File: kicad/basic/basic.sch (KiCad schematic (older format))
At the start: 20 parts, among them P2 CONN_01X15, P3 CONN_01X15, P4 CONN_01X06, P5 CONN_01X01, P6 CONN_01X01, P7 CONN_01X01, P8 CONN_01X01, P9 CONN_01X06, SW1 SW_PUSH, SW2 SW_PUSH

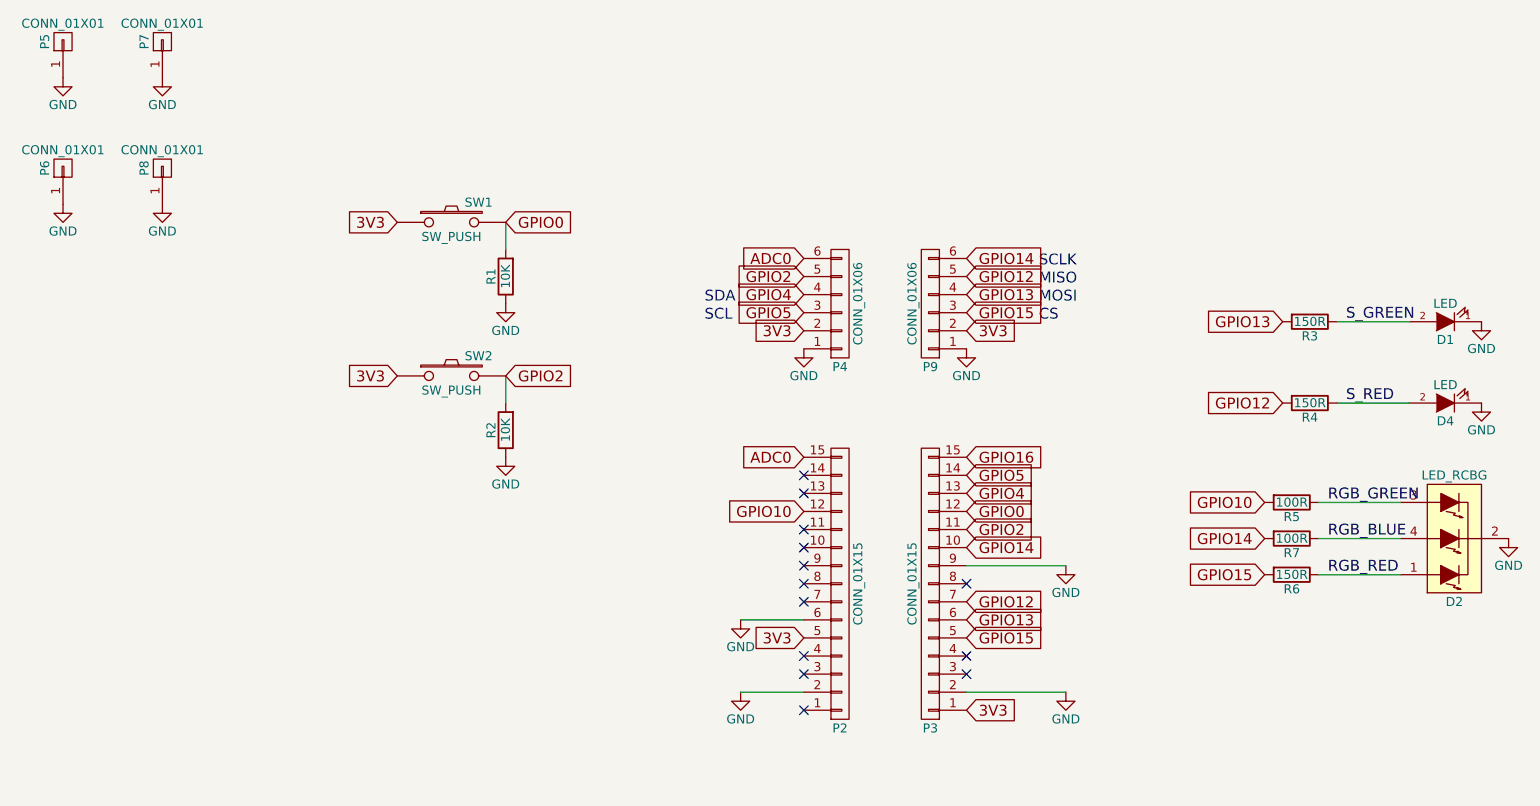
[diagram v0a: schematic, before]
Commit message: I2C & SPI on the headers
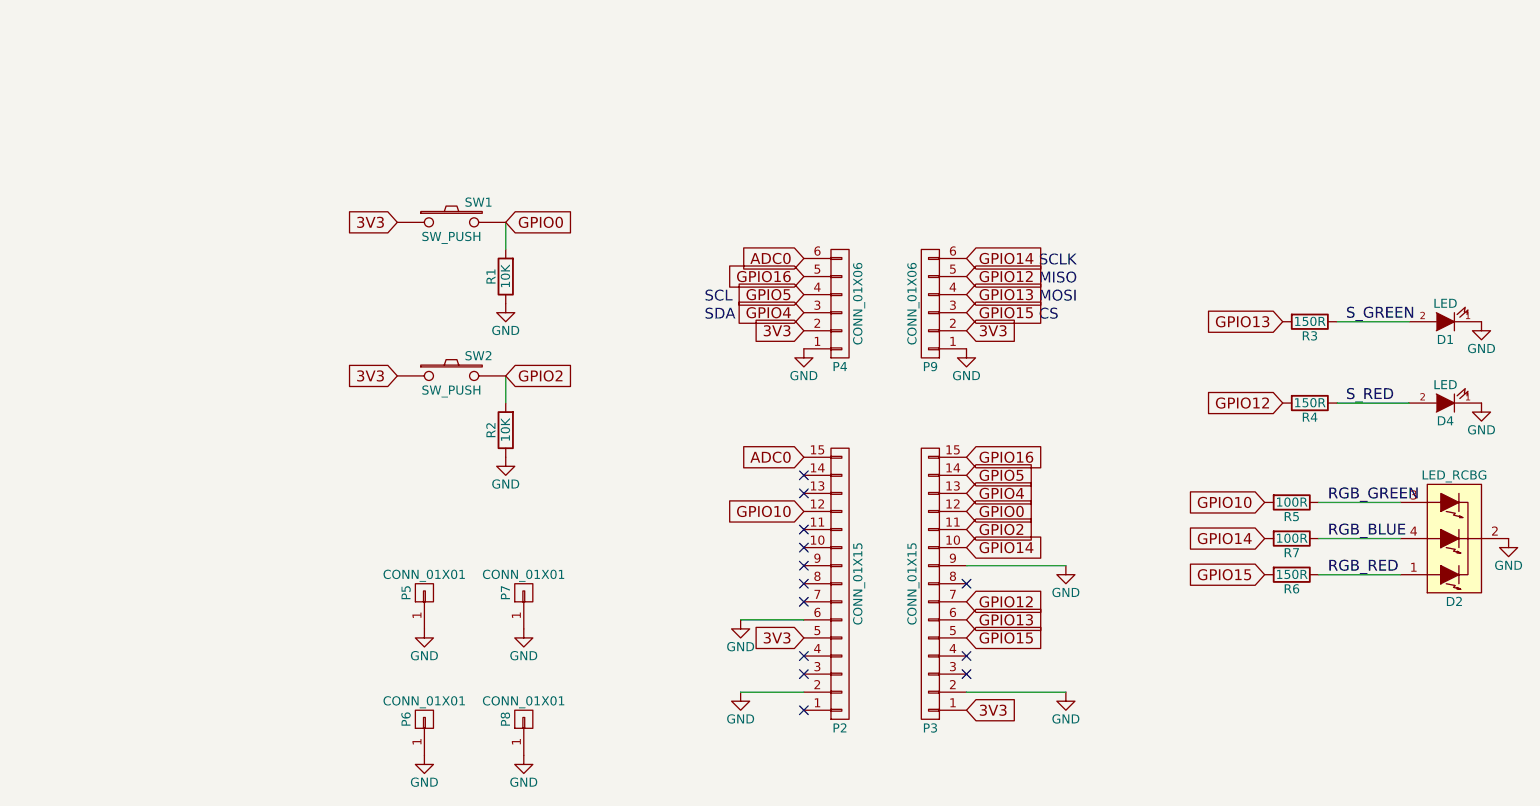
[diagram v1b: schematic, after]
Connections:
- net GPIO16: now also P4.5 (P5)
- net GPIO2: no longer P4.5 (P5)
- net GPIO4: now also P4.3 (P3); no longer P4.4 (P4)
- net GPIO5: now also P4.4 (P4); no longer P4.3 (P3)
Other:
- moved on the sheet: P5, P6, P7, P8
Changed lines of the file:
@@
 L CONN_01X01 P5
 U 1 1 570F7699
-P 1400 1200
-F 0 "P5" H 1400 1300 50  0000 C CNN
-F 1 "CONN_01X01" V 1500 1200 50  0000 C CNN
-F 2 "Mounting_Holes:MountingHole_3.2mm_M3_ISO14580_Pad" H 1400 1200 50  0001 C CNN
-F 3 "" H 1400 1200 50  0000 C CNN
-	1    1400 1200
+P 3400 4250
+F 0 "P5" H 3400 4350 50  0000 C CNN
+F 1 "CONN_01X01" V 3500 4250 50  0000 C CNN
+F 2 "Mounting_Holes:MountingHole_3.2mm_M3_ISO14580_Pad" H 3400 4250 50  0001 C CNN
+F 3 "" H 3400 4250 50  0000 C CNN
+	1    3400 4250
 	0    -1   -1   0
 $EndComp
@@
 L GND #PWR02
 U 1 1 570F7753
-P 1400 1400
-F 0 "#PWR02" H 1400 1150 50  0001 C CNN
-F 1 "GND" H 1400 1250 50  0000 C CNN
-F 2 "" H 1400 1400 50  0000 C CNN
-F 3 "" H 1400 1400 50  0000 C CNN
-	1    1400 1400
+P 3400 4450
+F 0 "#PWR02" H 3400 4200 50  0001 C CNN
+F 1 "GND" H 3400 4300 50  0000 C CNN
+F 2 "" H 3400 4450 50  0000 C CNN
+F 3 "" H 3400 4450 50  0000 C CNN
+	1    3400 4450
 	1    0    0    -1
 $EndComp
@@
 L CONN_01X01 P7
 U 1 1 570F783F
-P 1950 1200
-F 0 "P7" H 1950 1300 50  0000 C CNN
-F 1 "CONN_01X01" V 2050 1200 50  0000 C CNN
-F 2 "Mounting_Holes:MountingHole_3.2mm_M3_ISO14580_Pad" H 1950 1200 50  0001 C CNN
-F 3 "" H 1950 1200 50  0000 C CNN
-	1    1950 1200
+P 3950 4250
+F 0 "P7" H 3950 4350 50  0000 C CNN
+F 1 "CONN_01X01" V 4050 4250 50  0000 C CNN
+F 2 "Mounting_Holes:MountingHole_3.2mm_M3_ISO14580_Pad" H 3950 4250 50  0001 C CNN
+F 3 "" H 3950 4250 50  0000 C CNN
+	1    3950 4250
 	0    -1   -1   0
 $EndComp
@@
 L GND #PWR03
 U 1 1 570F7845
-P 1950 1400
-F 0 "#PWR03" H 1950 1150 50  0001 C CNN
-F 1 "GND" H 1950 1250 50  0000 C CNN
-F 2 "" H 1950 1400 50  0000 C CNN
-F 3 "" H 1950 1400 50  0000 C CNN
-	1    1950 1400
+P 3950 4450
+F 0 "#PWR03" H 3950 4200 50  0001 C CNN
+F 1 "GND" H 3950 4300 50  0000 C CNN
+F 2 "" H 3950 4450 50  0000 C CNN
+F 3 "" H 3950 4450 50  0000 C CNN
+	1    3950 4450
 	1    0    0    -1
 $EndComp
@@
 L CONN_01X01 P6
 U 1 1 570F78B5
-P 1400 1900
-F 0 "P6" H 1400 2000 50  0000 C CNN
-F 1 "CONN_01X01" V 1500 1900 50  0000 C CNN
-F 2 "Mounting_Holes:MountingHole_3.2mm_M3_ISO14580_Pad" H 1400 1900 50  0001 C CNN
-F 3 "" H 1400 1900 50  0000 C CNN
-	1    1400 1900
+P 3400 4950
+F 0 "P6" H 3400 5050 50  0000 C CNN
+F 1 "CONN_01X01" V 3500 4950 50  0000 C CNN
+F 2 "Mounting_Holes:MountingHole_3.2mm_M3_ISO14580_Pad" H 3400 4950 50  0001 C CNN
+F 3 "" H 3400 4950 50  0000 C CNN
+	1    3400 4950
 	0    -1   -1   0
 $EndComp
@@
 L GND #PWR04
 U 1 1 570F78BB
-P 1400 2100
-F 0 "#PWR04" H 1400 1850 50  0001 C CNN
-F 1 "GND" H 1400 1950 50  0000 C CNN
-F 2 "" H 1400 2100 50  0000 C CNN
-F 3 "" H 1400 2100 50  0000 C CNN
-	1    1400 2100
+P 3400 5150
+F 0 "#PWR04" H 3400 4900 50  0001 C CNN
+F 1 "GND" H 3400 5000 50  0000 C CNN
+F 2 "" H 3400 5150 50  0000 C CNN
+F 3 "" H 3400 5150 50  0000 C CNN
+	1    3400 5150
 	1    0    0    -1
 $EndComp
@@
 L CONN_01X01 P8
 U 1 1 570F78C1
-P 1950 1900
-F 0 "P8" H 1950 2000 50  0000 C CNN
-F 1 "CONN_01X01" V 2050 1900 50  0000 C CNN
-F 2 "Mounting_Holes:MountingHole_3.2mm_M3_ISO14580_Pad" H 1950 1900 50  0001 C CNN
-F 3 "" H 1950 1900 50  0000 C CNN
-	1    1950 1900
+P 3950 4950
+F 0 "P8" H 3950 5050 50  0000 C CNN
+F 1 "CONN_01X01" V 4050 4950 50  0000 C CNN
+F 2 "Mounting_Holes:MountingHole_3.2mm_M3_ISO14580_Pad" H 3950 4950 50  0001 C CNN
+F 3 "" H 3950 4950 50  0000 C CNN
+	1    3950 4950
 	0    -1   -1   0
 $EndComp
@@
 L GND #PWR05
 U 1 1 570F78C7
-P 1950 2100
-F 0 "#PWR05" H 1950 1850 50  0001 C CNN
-F 1 "GND" H 1950 1950 50  0000 C CNN
-F 2 "" H 1950 2100 50  0000 C CNN
-F 3 "" H 1950 2100 50  0000 C CNN
-	1    1950 2100
+P 3950 5150
+F 0 "#PWR05" H 3950 4900 50  0001 C CNN
+F 1 "GND" H 3950 5000 50  0000 C CNN
+F 2 "" H 3950 5150 50  0000 C CNN
+F 3 "" H 3950 5150 50  0000 C CNN
+	1    3950 5150
 	1    0    0    -1
 $EndComp
@@
 GPIO14
 Text GLabel 5500 2600 0    60   Input ~ 0
+GPIO5
+Text GLabel 5500 2700 0    60   Input ~ 0
 GPIO4
-Text GLabel 5500 2700 0    60   Input ~ 0
-GPIO5
 NoConn ~ 6400 4200
 Text GLabel 8050 3750 0    60   Input ~ 0
@@
 GPIO14
 Text GLabel 5500 2500 0    60   Input ~ 0
-GPIO2
+GPIO16
 Text GLabel 5500 2800 0    60   Input ~ 0
 3V3
@@
 Text Notes 6800 2750 0    60   ~ 0
 CS
+Text Notes 4950 2750 0    60   ~ 0
+SDA
 Text Notes 4950 2650 0    60   ~ 0
-SDA
-Text Notes 4950 2750 0    60   ~ 0
 SCL
 Text GLabel 6400 3700 2    60   Input ~ 0

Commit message: Pin tweaks
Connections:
- net GPIO10: now also R7.2; no longer R5.2
- net GPIO14: now also P3.8 (P8), R5.2; no longer P3.10 (P10), R7.2
- no-connect marks 13 -> 12
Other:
- note added: "3V3"
- note added: "D0"
- note added: "D1"
- note added: "D2"
- note added: "D3"
- note added: "D4"
- note added: "D5"
- note added: "D6"
- note added: "D7"
- note added: "D8"
- note added: "RX"
- note added: "SD3"
- note added: "TX"
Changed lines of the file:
@@
 L GND #PWR09
 U 1 1 570FA0BF
-P 6950 4100
-F 0 "#PWR09" H 6950 3850 50  0001 C CNN
-F 1 "GND" H 6950 3950 50  0000 C CNN
-F 2 "" H 6950 4100 50  0000 C CNN
-F 3 "" H 6950 4100 50  0000 C CNN
-	1    6950 4100
+P 7150 4100
+F 0 "#PWR09" H 7150 3850 50  0001 C CNN
+F 1 "GND" H 7150 3950 50  0000 C CNN
+F 2 "" H 7150 4100 50  0000 C CNN
+F 3 "" H 7150 4100 50  0000 C CNN
+	1    7150 4100
 	1    0    0    -1
 $EndComp
@@
 	6400 4800 6950 4800
 Wire Wire Line
-	6400 4100 6950 4100
+	6400 4100 7150 4100
 NoConn ~ 5500 3600
 NoConn ~ 5500 3700
@@
 Text GLabel 5500 2700 0    60   Input ~ 0
 GPIO4
-NoConn ~ 6400 4200
+Text GLabel 8050 3950 0    60   Input ~ 0
+GPIO10
 Text GLabel 8050 3750 0    60   Input ~ 0
-GPIO10
-Text GLabel 8050 3950 0    60   Input ~ 0
 GPIO14
 Text GLabel 8050 4150 0    60   Input ~ 0
@@
 	0    1    1    0
 $EndComp
-Text GLabel 6400 4000 2    60   Input ~ 0
+Text GLabel 6400 4200 2    60   Input ~ 0
 GPIO14
 Text GLabel 5500 2500 0    60   Input ~ 0
@@
 NoConn ~ 6400 4600
 NoConn ~ 6400 4700
+Text Notes 6850 3550 0    60   ~ 0
+D0
+Text Notes 6850 3650 0    60   ~ 0
+D1
+Text Notes 6850 3750 0    60   ~ 0
+D2
+Text Notes 6850 3850 0    60   ~ 0
+D3
+Text Notes 6850 3950 0    60   ~ 0
+D4
+Text Notes 6850 4050 0    60   ~ 0
+3V3
+Text Notes 6850 4250 0    60   ~ 0
+D5
+Text Notes 6850 4350 0    60   ~ 0
+D6
+Text Notes 6850 4450 0    60   ~ 0
+D7
+Text Notes 6850 4550 0    60   ~ 0
+D8
+Text Notes 6850 4650 0    60   ~ 0
+RX
+Text Notes 6850 4750 0    60   ~ 0
+TX
+Text Notes 4900 3850 0    60   ~ 0
+SD3
 $EndSCHEMATC

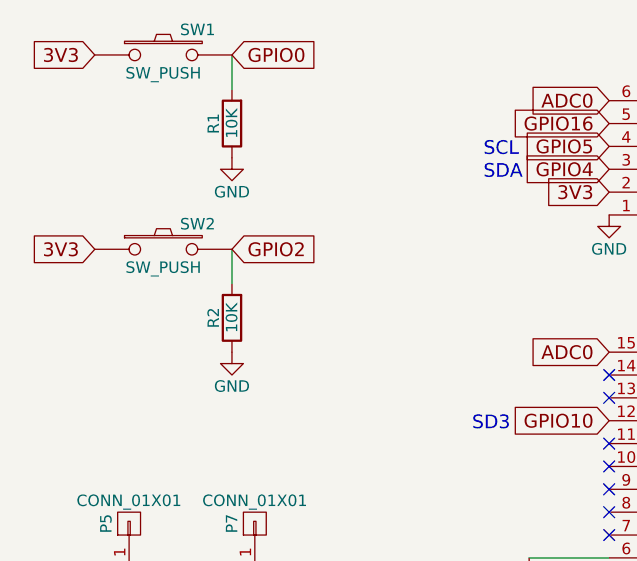
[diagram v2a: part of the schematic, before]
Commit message: Internal pullup on the switches
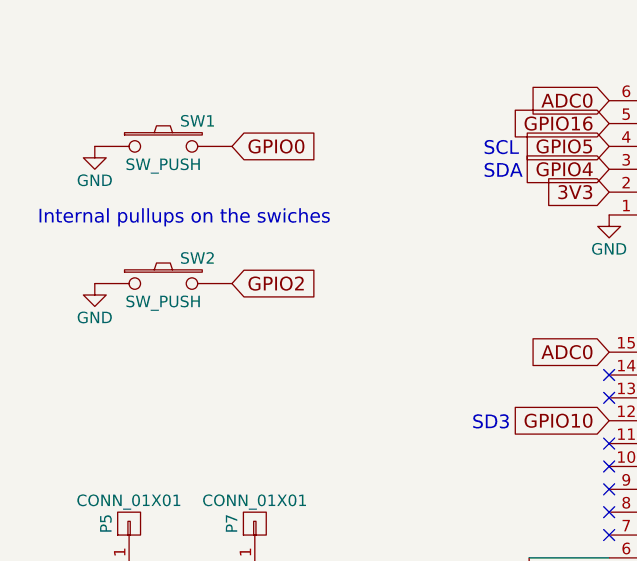
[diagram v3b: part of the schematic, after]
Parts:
- removed R1, R2: 10K, Resistors_ThroughHole:Resistor_Horizontal_RM10mm, symbol R
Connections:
- net 3V3: no longer SW1.1, SW2.1
- net GND: now also SW1.1, SW2.1
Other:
- note added: "Internal pullups on the swiches"
- moved on the sheet: SW1, SW2
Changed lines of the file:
@@
 L SW_PUSH SW1
 U 1 1 570F9210
-P 3550 2200
-F 0 "SW1" H 3700 2310 50  0000 C CNN
-F 1 "SW_PUSH" H 3550 2120 50  0000 C CNN
-F 2 "Buttons_Switches_ThroughHole:SW_PUSH_SMALL" H 3550 2200 50  0001 C CNN
-F 3 "" H 3550 2200 50  0000 C CNN
-	1    3550 2200
+P 3550 2600
+F 0 "SW1" H 3700 2710 50  0000 C CNN
+F 1 "SW_PUSH" H 3550 2520 50  0000 C CNN
+F 2 "Buttons_Switches_ThroughHole:SW_PUSH_SMALL" H 3550 2600 50  0001 C CNN
+F 3 "" H 3550 2600 50  0000 C CNN
+	1    3550 2600
 	1    0    0    -1
 $EndComp
@@
 L SW_PUSH SW2
 U 1 1 570F927F
-P 3550 3050
-F 0 "SW2" H 3700 3160 50  0000 C CNN
-F 1 "SW_PUSH" H 3550 2970 50  0000 C CNN
-F 2 "Buttons_Switches_ThroughHole:SW_PUSH_SMALL" H 3550 3050 50  0001 C CNN
-F 3 "" H 3550 3050 50  0000 C CNN
-	1    3550 3050
+P 3550 3200
+F 0 "SW2" H 3700 3310 50  0000 C CNN
+F 1 "SW_PUSH" H 3550 3120 50  0000 C CNN
+F 2 "Buttons_Switches_ThroughHole:SW_PUSH_SMALL" H 3550 3200 50  0001 C CNN
+F 3 "" H 3550 3200 50  0000 C CNN
+	1    3550 3200
 	1    0    0    -1
 $EndComp
@@
 	5150 4800 5500 4800
 $Comp
-L R R1
-U 1 1 570FAF94
-P 3850 2500
-F 0 "R1" V 3930 2500 50  0000 C CNN
-F 1 "10K" V 3850 2500 50  0000 C CNN
-F 2 "Resistors_ThroughHole:Resistor_Horizontal_RM10mm" V 3780 2500 50  0001 C CNN
-F 3 "" H 3850 2500 50  0000 C CNN
-	1    3850 2500
-	-1   0    0    1
-$EndComp
-$Comp
-L R R2
-U 1 1 570FB0D0
-P 3850 3350
-F 0 "R2" V 3930 3350 50  0000 C CNN
-F 1 "10K" V 3850 3350 50  0000 C CNN
-F 2 "Resistors_ThroughHole:Resistor_Horizontal_RM10mm" V 3780 3350 50  0001 C CNN
-F 3 "" H 3850 3350 50  0000 C CNN
-	1    3850 3350
-	-1   0    0    1
-$EndComp
-Wire Wire Line
-	3850 2350 3850 2200
-Wire Wire Line
-	3850 3050 3850 3200
-$Comp
 L GND #PWR012
 U 1 1 570FB498
-P 3850 2650
-F 0 "#PWR012" H 3850 2400 50  0001 C CNN
-F 1 "GND" H 3850 2500 50  0000 C CNN
-F 2 "" H 3850 2650 50  0000 C CNN
-F 3 "" H 3850 2650 50  0000 C CNN
-	1    3850 2650
+P 3250 2600
+F 0 "#PWR012" H 3250 2350 50  0001 C CNN
+F 1 "GND" H 3250 2450 50  0000 C CNN
+F 2 "" H 3250 2600 50  0000 C CNN
+F 3 "" H 3250 2600 50  0000 C CNN
+	1    3250 2600
 	1    0    0    -1
 $EndComp
@@
 L GND #PWR013
 U 1 1 570FB53B
-P 3850 3500
-F 0 "#PWR013" H 3850 3250 50  0001 C CNN
-F 1 "GND" H 3850 3350 50  0000 C CNN
-F 2 "" H 3850 3500 50  0000 C CNN
-F 3 "" H 3850 3500 50  0000 C CNN
-	1    3850 3500
-	1    0    0    -1
-$EndComp
-Text GLabel 3250 3050 0    60   Input ~ 0
-3V3
-Text GLabel 3250 2200 0    60   Input ~ 0
-3V3
+P 3250 3200
+F 0 "#PWR013" H 3250 2950 50  0001 C CNN
+F 1 "GND" H 3250 3050 50  0000 C CNN
+F 2 "" H 3250 3200 50  0000 C CNN
+F 3 "" H 3250 3200 50  0000 C CNN
+	1    3250 3200
+	1    0    0    -1
+$EndComp
 $Comp
 L CONN_01X06 P4
@@
 Text GLabel 8150 2750 0    60   Input ~ 0
 GPIO13
-Text GLabel 3850 2200 2    60   Input ~ 0
+Text GLabel 3850 2600 2    60   Input ~ 0
 GPIO0
-Text GLabel 3850 3050 2    60   Input ~ 0
+Text GLabel 3850 3200 2    60   Input ~ 0
 GPIO2
 $Comp
@@
 Text Notes 4900 3850 0    60   ~ 0
 SD3
+Text Notes 3000 2950 0    60   ~ 0
+Internal pullups on the swiches
 $EndSCHEMATC
